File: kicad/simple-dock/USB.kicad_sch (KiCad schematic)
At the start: 2 parts, among them J5 USB_A, J6 USB_A

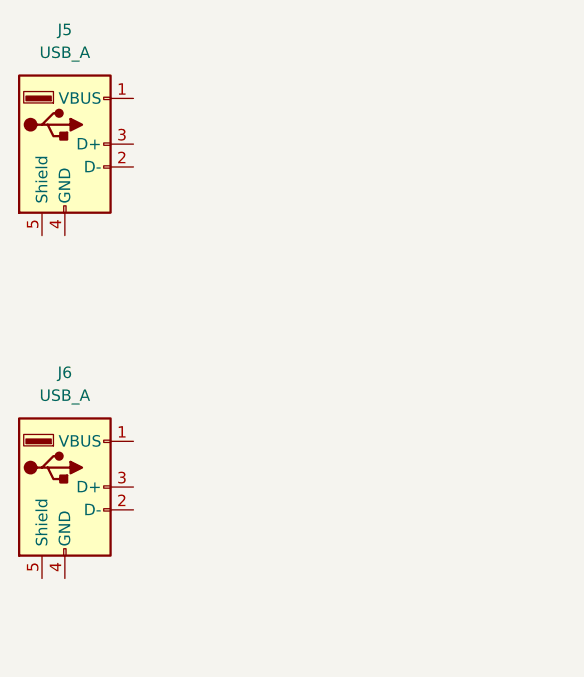
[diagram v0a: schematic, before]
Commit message: kicad add usb
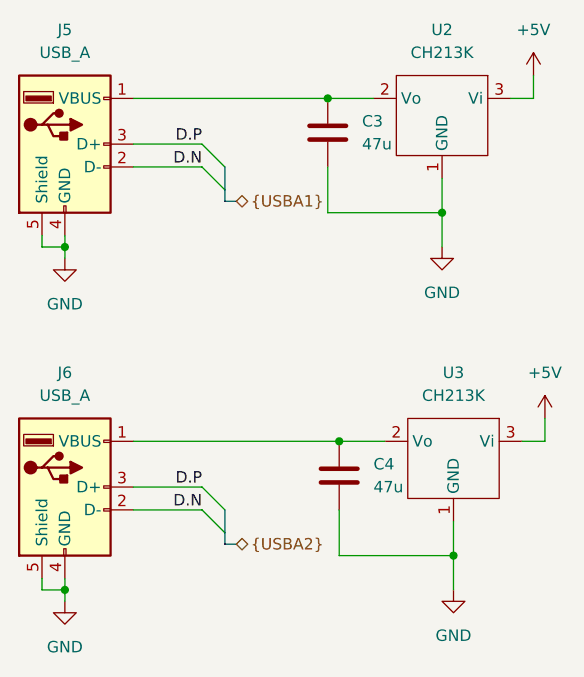
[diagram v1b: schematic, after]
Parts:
- added C3, C4: 47u, symbol Device:C
- added U2, U3: CH213K, Package_TO_SOT_SMD:SOT-23-3, symbol ch213k:CH213K
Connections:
- net at J6.1 (VBUS): now also C4.1, U3.2 (Vo)
- net D.N: now reaches J6.2 (D-)
- net D.N: now also J5.2 (D-)
- net D.P: now reaches J6.3 (D+)
- net D.P: now also J5.3 (D+)
- net GND: now reaches J6.4 (GND)
- net GND: now also J5.4 (GND), J5.5 (Shield), J6.5 (Shield), C3.2, C4.2, U2.1 (GND), U3.1 (GND)
- net at J5.1 (VBUS): now also C3.1, U2.2 (Vo)
- new net +5V: U2.3 (Vi), U3.3 (Vi)
